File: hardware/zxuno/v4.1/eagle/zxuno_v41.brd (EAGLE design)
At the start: 86 x 56 mm, 105 parts, among them T1 BC846, U1 6SLX9TQG144, U2 FLASH-SPI-25XXSMD1, U4 AD724, U5 50MHz, U6 3.3V, U7 1.2V, Y1 3.58M, Y2 4.43M

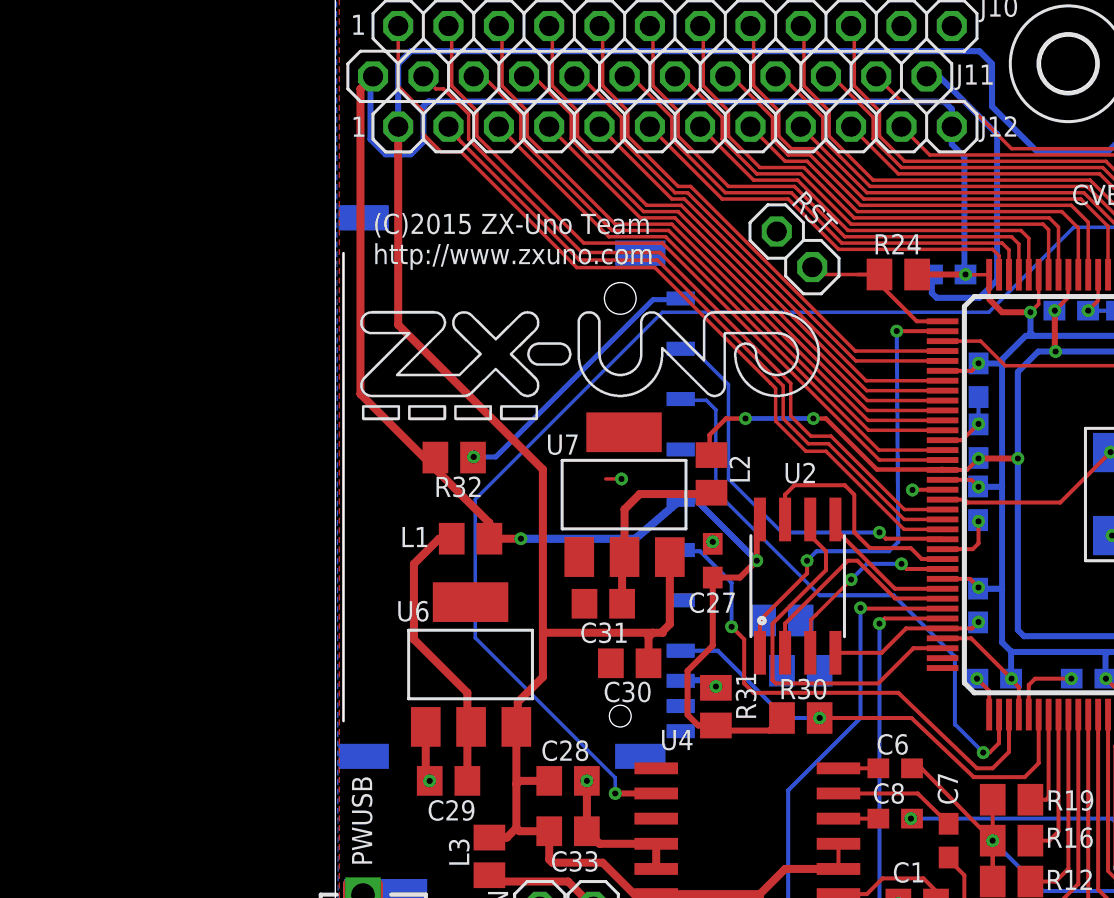
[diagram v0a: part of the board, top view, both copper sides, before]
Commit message: 
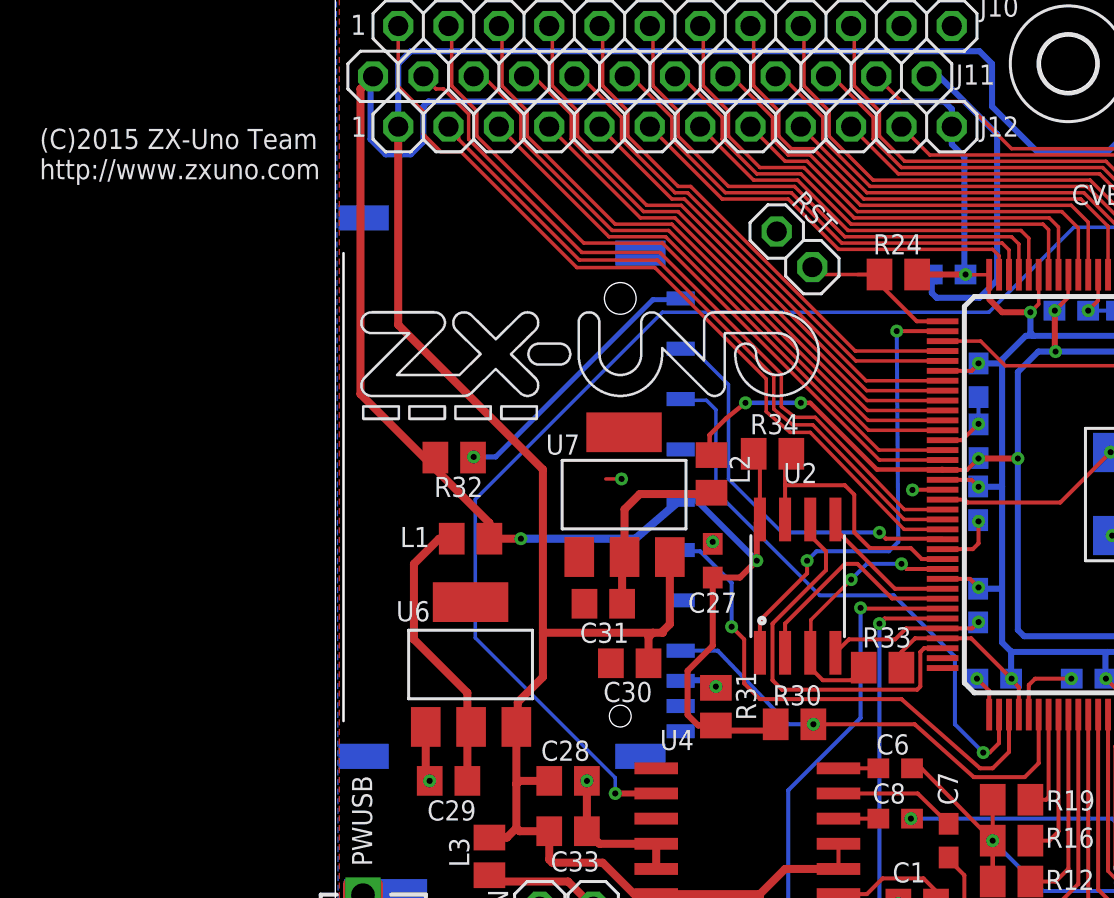
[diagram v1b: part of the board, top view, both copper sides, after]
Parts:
- moved R34 8.43 mm to (22.1, 32.4), flipped to the top
- moved R33 4.13 mm to (27.6, 21.6), flipped to the top, turned to 0 degrees
- moved R30 0.45 mm to (23.2, 18.7)
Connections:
- removed net VCC: R33.2, R34.2
- net 3.3V: now also R33.2, R34.2
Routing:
- net 3.3V: track 288.7 -> 294.8 mm
- net FLASH_WP: track 9.60 -> 13.6 mm
- net FLASH_HOLD: track 12.1 -> 14.2 mm
- net FLASH_SCK: track 18.9 -> 20.2 mm
- net 1.2V: track 76.9 -> 77.5 mm

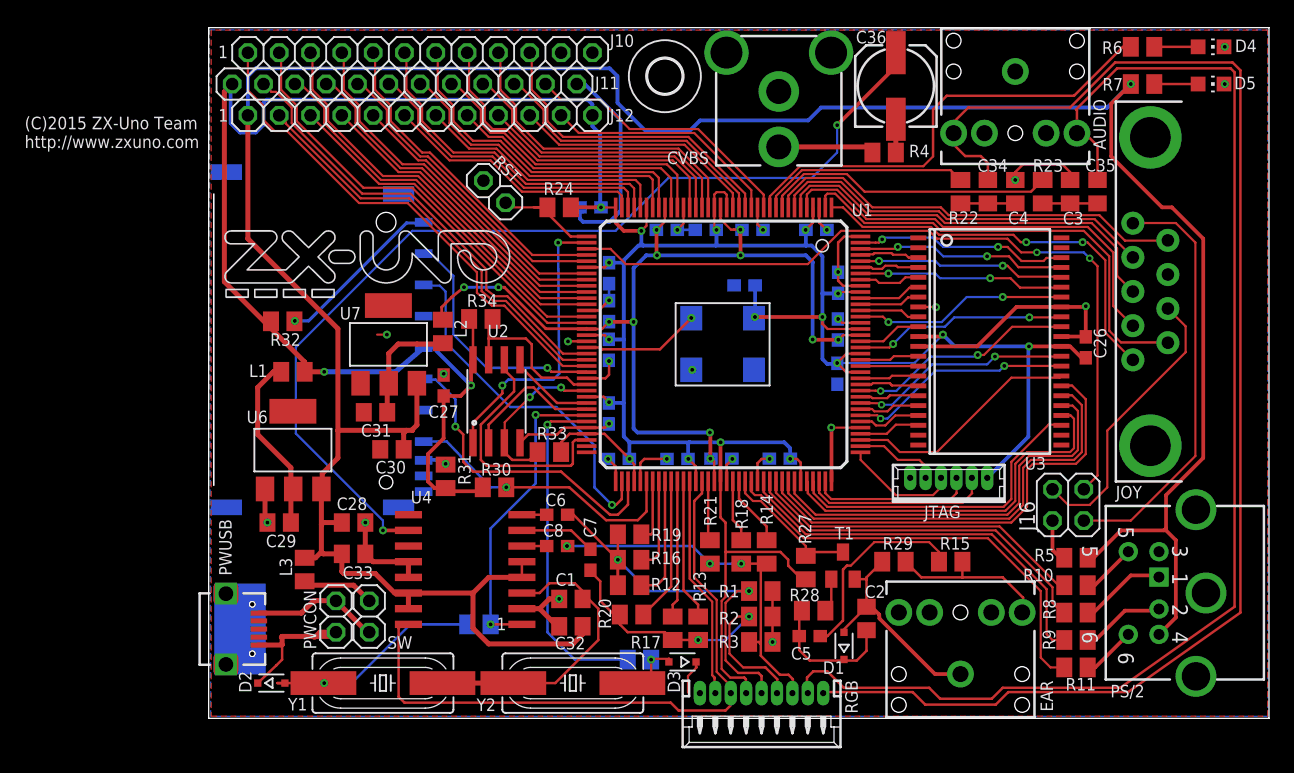
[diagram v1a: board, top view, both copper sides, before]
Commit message: Huellas arregladas con serigrafía en contorno
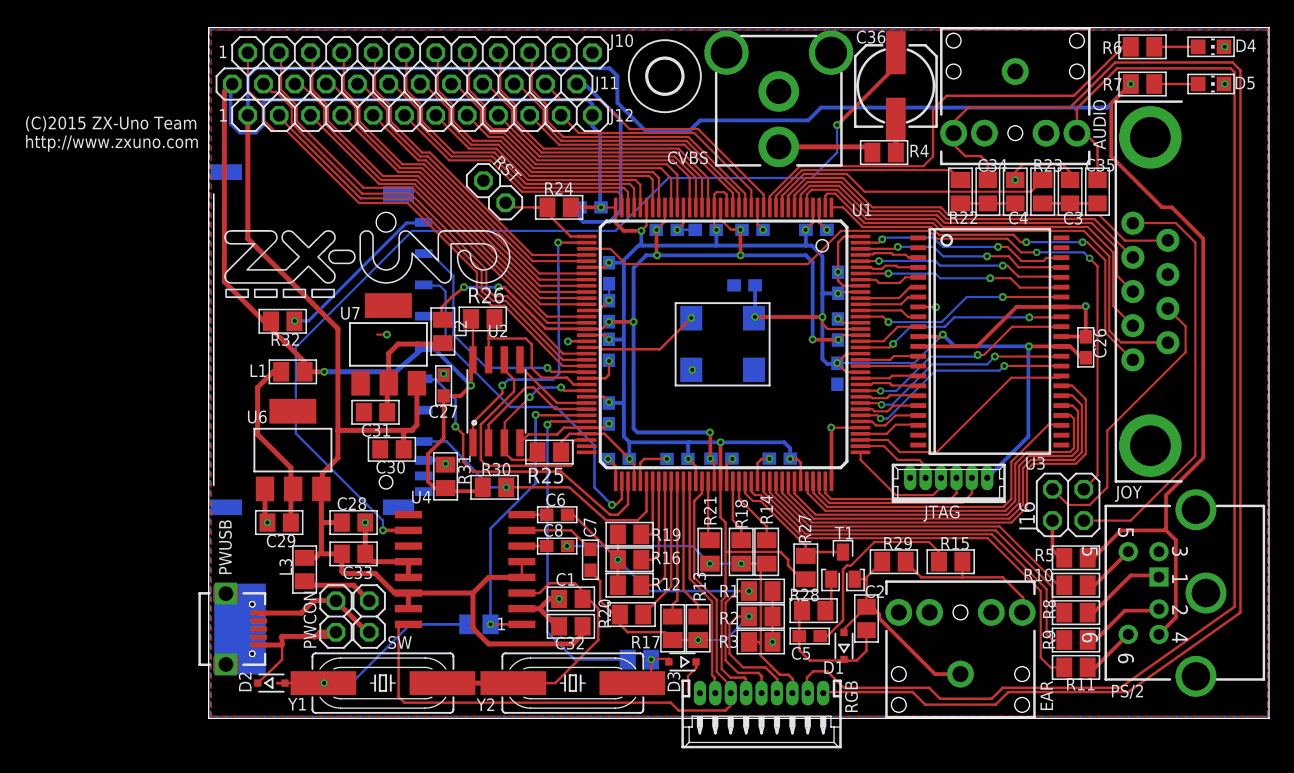
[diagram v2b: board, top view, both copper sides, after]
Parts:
- R25, R26: value 10K -> 2K
- R33, R34: value 2K -> 10K; device resistor:M0805 -> rcl:M0805
- moved R34 30.5 mm to (34.9, 4.76), flipped to the bottom, turned to 0 degrees
- moved R26 30.4 mm to (22.2, 32.4), flipped to the top
- moved R25 15.1 mm to (27.6, 21.6), flipped to the top, turned to 180 degrees
- moved R33 15.1 mm to (21.9, 7.62), flipped to the bottom
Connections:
- net 3.3V: now also R25.1, R26.1; no longer R33.2, R34.2
- net FLASH_HOLD: now also R26.2; no longer R34.1
- net FLASH_WP: now also R25.2; no longer R33.1
- net N$24: now also R34.1; no longer R26.1
- net N$25: now also R33.2; no longer R25.2
- net STDN: now also R33.1; no longer R25.1
- net STDNB: now also R34.2; no longer R26.2
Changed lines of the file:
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@@
 <attribute name="VALUE" x="35.2425" y="7.0485" size="1.27" layer="27" ratio="10" rot="R180"/>
 </element>
-<element name="R25" library="rcl" package="M0805" value="10K" x="21.9075" y="7.62" smashed="yes" rot="MR0">
+<element name="R33" library="rcl" package="M0805" value="10K" x="21.9075" y="7.62" smashed="yes" rot="MR0">
 <attribute name="NAME" x="22.9235" y="8.763" size="1.016" layer="26" font="vector" ratio="15" rot="MR0"/>
 <attribute name="VALUE" x="23.1775" y="5.08" size="1.27" layer="28" rot="MR0"/>
 </element>
-<element name="R26" library="rcl" package="M0805" value="10K" x="34.925" y="4.7625" smashed="yes" rot="MR0">
+<element name="R34" library="rcl" package="M0805" value="10K" x="34.925" y="4.7625" smashed="yes" rot="MR0">
 <attribute name="NAME" x="36.195" y="6.0325" size="1.016" layer="26" font="vector" ratio="15" rot="MR0"/>
 <attribute name="VALUE" x="36.195" y="2.2225" size="1.27" layer="28" rot="MR0"/>
@@
 <attribute name="VALUE" x="72.23125" y="21.74875" size="1.27" layer="27" rot="R180"/>
 </element>
-<element name="R33" library="resistor" package="M0805" value="2K" x="27.6225" y="21.59" smashed="yes">
-<attribute name="NAME" x="26.6065" y="22.606" size="1.016" layer="25" font="vector" ratio="15"/>
-<attribute name="VALUE" x="26.6065" y="19.304" size="1.27" layer="27"/>
-</element>
-<element name="R34" library="resistor" package="M0805" value="2K" x="22.06625" y="32.385" smashed="yes" rot="R180">
-<attribute name="NAME" x="23.39975" y="34.38525" size="1.016" layer="25" font="vector" ratio="15" rot="R180"/>
-<attribute name="VALUE" x="23.08225" y="34.671" size="1.27" layer="27" rot="R180"/>
-</element>
+<element name="R25" library="rcl" package="M0805" value="2K" x="27.6225" y="21.59" rot="R180"/>
+<element name="R26" library="rcl" package="M0805" value="2K" x="22.225" y="32.385"/>
 </elements>
 <signals>
@@
 <wire x1="66.46625" y1="30.1125" x2="66.46625" y2="22.83375" width="0.3048" layer="16"/>
 <wire x1="66.46625" y1="22.83375" x2="63.1325" y2="19.5" width="0.3048" layer="16"/>
-<contactref element="R33" pad="2"/>
-<contactref element="R34" pad="2"/>
 <wire x1="21.43125" y1="29.0703" x2="21.43125" y2="31.7525" width="0.2032" layer="1"/>
-<wire x1="21.43125" y1="31.7525" x2="21.11625" y2="32.385" width="0.2032" layer="1"/>
 <wire x1="30.65125" y1="23.07125" x2="29.2625" y2="23.07125" width="0.2032" layer="1"/>
 <wire x1="29.2625" y1="23.07125" x2="28.575" y2="22.38375" width="0.2032" layer="1"/>
 <wire x1="28.575" y1="22.38375" x2="28.575" y2="21.5925" width="0.2032" layer="1"/>
-<wire x1="28.575" y1="21.5925" x2="28.5725" y2="21.59" width="0.2032" layer="1"/>
+<contactref element="R25" pad="1"/>
+<contactref element="R26" pad="1"/>
+<wire x1="21.275" y1="32.385" x2="21.275" y2="31.90875" width="0.2032" layer="1"/>
+<wire x1="21.275" y1="31.90875" x2="21.43125" y2="31.7525" width="0.2032" layer="1"/>
 <wire x1="51.038125" y1="34.44875" x2="51.038125" y2="34.471875" width="0" layer="19" extent="1-16"/>
 <wire x1="41.15265625" y1="39.608125" x2="41.17578125" y2="39.608125" width="0" layer="19" extent="1-16"/>
@@
 <wire x1="32.464375" y1="36.9490625" x2="32.464375" y2="36.94578125" width="0" layer="19" extent="16-16"/>
 <wire x1="50.97859375" y1="28.79" x2="50.95875" y2="28.813125" width="0" layer="19" extent="1-16"/>
+<wire x1="28.5725" y1="21.59" x2="28.575" y2="21.5925" width="0.2032" layer="1"/>
 </signal>
 <signal name="XA0">
@@
 <wire x1="26.19375" y1="28.41625" x2="26.9875" y2="27.6225" width="0.2032" layer="1"/>
 <wire x1="26.9875" y1="27.6225" x2="29.05125" y2="27.6225" width="0.2032" layer="1"/>
-<contactref element="R34" pad="1"/>
 <wire x1="22.70125" y1="29.0703" x2="22.70125" y2="30.7975" width="0.2032" layer="1"/>
 <wire x1="22.70125" y1="30.7975" x2="22.70125" y2="32.3825" width="0.2032" layer="1"/>
-<wire x1="22.70125" y1="32.3825" x2="23.01625" y2="32.385" width="0.2032" layer="1"/>
+<contactref element="R26" pad="2"/>
+<wire x1="23.175" y1="32.385" x2="22.70375" y2="32.385" width="0.2032" layer="1"/>
+<wire x1="22.70375" y1="32.385" x2="22.70125" y2="32.3825" width="0.2032" layer="1"/>
 </signal>
 <signal name="FLASH_SCK">
@@
 <wire x1="24.003" y1="24.003" x2="24.003" y2="23.20925" width="0.1778" layer="1"/>
 <wire x1="24.003" y1="23.20925" x2="23.97125" y2="23.1775" width="0.1778" layer="1"/>
-<contactref element="R33" pad="1"/>
 <wire x1="24.60625" y1="20.955" x2="23.97125" y2="21.59" width="0.2032" layer="1"/>
 <wire x1="23.97125" y1="21.59" x2="23.97125" y2="22.3393" width="0.2032" layer="1"/>
 <wire x1="24.60625" y1="20.955" x2="26.0375" y2="20.955" width="0.2032" layer="1"/>
-<wire x1="26.0375" y1="20.955" x2="26.6725" y2="21.59" width="0.2032" layer="1"/>
+<contactref element="R25" pad="2"/>
+<wire x1="26.6725" y1="21.59" x2="26.0375" y2="20.955" width="0.2032" layer="1"/>
 </signal>
 <signal name="N$1">
@@
 <signal name="STDN">
 <contactref element="U4" pad="1"/>
-<contactref element="R25" pad="1"/>
+<contactref element="R33" pad="1"/>
 <contactref element="U1" pad="P66"/>
 <wire x1="30.65125" y1="24.57125" x2="26.54625" y2="24.57125" width="0.2032" layer="1"/>
@@
 </signal>
 <signal name="STDNB">
-<contactref element="R26" pad="2"/>
+<contactref element="R34" pad="2"/>
 <contactref element="U1" pad="P67"/>
 <wire x1="30.65125" y1="24.07125" x2="27.7225" y2="24.07125" width="0.2032" layer="1"/>
@@
 <signal name="N$24">
 <contactref element="Y2" pad="1"/>
-<contactref element="R26" pad="1"/>
+<contactref element="R34" pad="1"/>
 <via x="35.8775" y="4.7625" extent="1-16" drill="0.3048" diameter="0.6604"/>
 <wire x1="35.8775" y1="4.7625" x2="35.8775" y2="3.4925" width="0.2032" layer="1"/>
@@
 <signal name="N$25">
 <contactref element="Y1" pad="1"/>
-<contactref element="R25" pad="2"/>
+<contactref element="R33" pad="2"/>
 <wire x1="9.30275" y1="2.8575" x2="5.5625" y2="2.8575" width="0.2032" layer="1"/>
 <wire x1="20.9575" y1="7.62" x2="16.35125" y2="7.62" width="0.2032" layer="16"/>

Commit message: Meto revisión 758 que tiene vías hacia SRAM
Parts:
- removed R33, R34: 10K, rcl:M0805
- CVBS: device ZX_UNO_0_15:RCA_JACK_RCJ-04X_-_DUPLICATE_1PRIMARY -> uzebox:RCA
- D1, D2, D3: device diode:SOD323-R -> adafruit:SOD-323F
- R25, R26: value 2K -> 10K
- moved R26 30.4 mm to (34.9, 4.76), flipped to the bottom
- moved R25 15.1 mm to (21.9, 7.62), flipped to the bottom, turned to 0 degrees
- moved C6 3.18 mm to (28.4, 13.3), turned to 270 degrees
- moved C8 2.62 mm to (28.9, 16.5)
- moved D1 0.72 mm to (51.4, 5.16), turned to 270 degrees
- moved D2 0.72 mm to (4.41, 2.62), turned to 180 degrees
- moved D3 0.45 mm to (38.8, 4.36), turned to 0 degrees
- moved R30 0.45 mm to (23.5, 19.1)
- moved L2 0.44 mm to (19.4, 31.4)
- moved R28 0.16 mm to (49.1, 8.89)
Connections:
- net 3.3V: no longer R25.1, R26.1
- net B: now also C8.2, R14.1, R18.1, R21.1, R3.1, RGB.7; no longer C6.2, R1.1, R12.1, R16.1, R19.1, RGB.5
- net B0: now also R21.2, U1.P88; no longer R19.2, U1.P79
- net B1: now also R18.2, U1.P92; no longer R16.2, U1.P80
- net B2: now also R14.2, U1.P93; no longer R12.2, U1.P81
- net FLASH_HOLD: no longer R26.2
- net FLASH_WP: no longer R25.2
- net GND: now also CVBS.GND, JTAG.2; no longer CVBS.4, JTAG.6
- net N$19: now also U4.8; no longer U4.6
- net N$22: now also U4.6; no longer U4.8
- net N$24: now also R26.1; no longer R34.1
- net N$25: now also R25.2; no longer R33.2
- net N$28: now also CVBS.SIG; no longer CVBS.3
- net R: now also C6.2, R1.1, R12.1, R16.1, R19.1, RGB.5; no longer C8.2, R14.1, R18.1, R21.1, R3.1, RGB.7
- net R0: now also R19.2, U1.P79; no longer R21.2, U1.P88
- net R1: now also R16.2, U1.P80; no longer R18.2, U1.P92
- net R2: now also R12.2, U1.P81; no longer R14.2, U1.P93
- net STDN: now also R25.1; no longer R33.1
- net STDNB: now also R26.2; no longer R34.2
- net TCK: now also JTAG.3; no longer JTAG.4
- net TDO: now also JTAG.4; no longer JTAG.2
- net TMS: now also JTAG.6; no longer JTAG.3
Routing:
- net GND: track 149.9 -> 141.4 mm
- net 3.3V: track 294.8 -> 288.5 mm
- net B: track 35.3 -> 30.4 mm, vias 2 -> 3
- net 5V: track 228.6 -> 233.3 mm
- net R: track 30.1 -> 34.6 mm, vias 3 -> 2
- net R2: track 5.71 -> 9.97 mm
- net B2: track 9.97 -> 5.71 mm
- net FLASH_WP: track 13.6 -> 9.60 mm
- net TMS: track 13.2 -> 9.41 mm
- net TDI: track 6.90 -> 10.6 mm
- net TDO: track 15.3 -> 12.6 mm
- net R1: track 5.06 -> 7.51 mm
- net B1: track 7.51 -> 5.06 mm
- net FLASH_HOLD: track 14.4 -> 12.1 mm
- net FLASH_SCK: track 20.2 -> 18.9 mm
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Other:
- board text added: "v4.1"
